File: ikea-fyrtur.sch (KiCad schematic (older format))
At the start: 43 parts, among them J1 EXT_CTRL, J2 MOTOR, J3 UART_TagConnect, J4 UART_2mm, J5 PWR, J6 I2C, J8 IO15, Q1 SS8050-G, Q2 SS8050-G, SW1 SW1_RST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

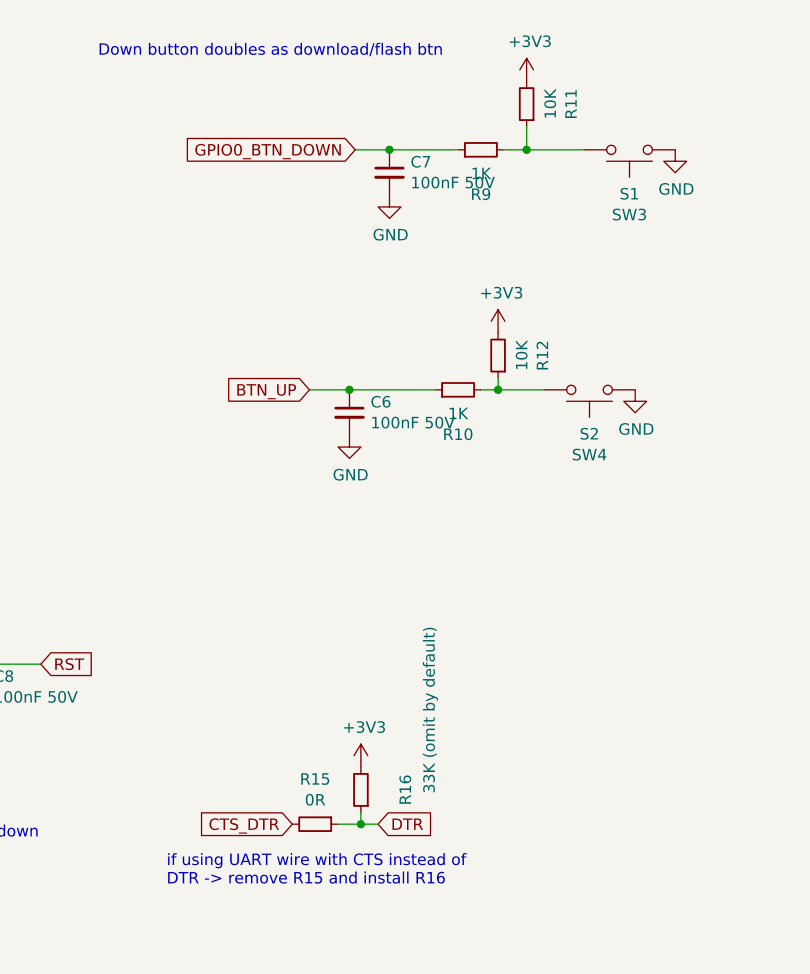
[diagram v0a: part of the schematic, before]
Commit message: - Change R9 from 1K to 120R (Setting GPIO0 line low via Down-Button may not lower voltage enough otherwise) - Added images, updated README - Change schematic revision to 0.71  (Resistor value change does not warrant change to the PCB)
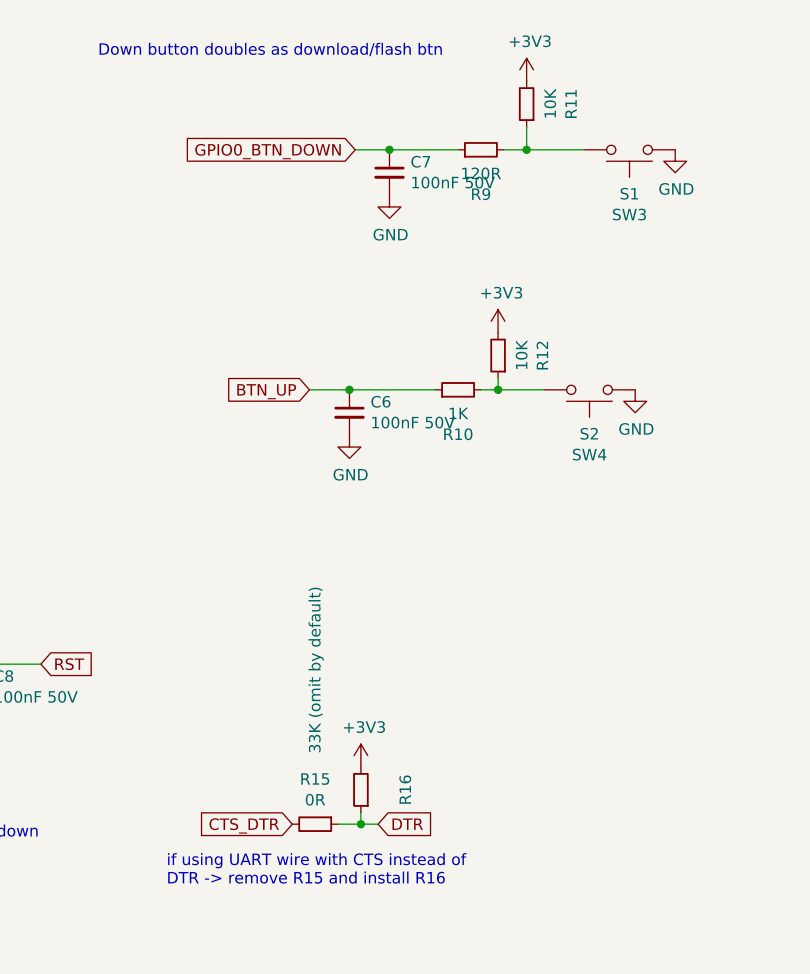
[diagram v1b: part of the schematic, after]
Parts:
- R9: value 1K -> 120R
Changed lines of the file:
@@
 Title "Ikea Fyrtur WiFi module"
 Date "2020-10-07"
-Rev "0.7"
+Rev "0.71"
 Comp "Marko Juhanne"
 Comment1 ""
@@
 P 6150 4000
 F 0 "R9" V 5954 4000 50  0000 C CNN
-F 1 "1K" V 6045 4000 50  0000 C CNN
+F 1 "120R" V 6045 4000 50  0000 C CNN
 F 2 "Resistor_SMD:R_0603_1608Metric" H 6150 4000 50  0001 C CNN
 F 3 "~" H 6150 4000 50  0001 C CNN
@@
 P 5625 6800
 F 0 "R16" V 5429 6800 50  0000 C CNN
-F 1 "33K (omit by default)" V 5325 6450 50  0000 C CNN
+F 1 "33K (omit by default)" V 5825 6275 50  0000 C CNN
 F 2 "Resistor_SMD:R_0603_1608Metric" H 5625 6800 50  0001 C CNN
 F 3 "~" H 5625 6800 50  0001 C CNN
